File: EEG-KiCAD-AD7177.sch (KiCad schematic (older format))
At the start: 52 parts, among them J1 Conn_01x06, J2 Conn_01x02, J3 Conn_01x02, U1 AD7177-2, U2 OPAMP, U3 NRF528XX-QFAA, U4 RP511Z331_3.3V, U5 XCL101A501-5V, X1 Crystal_GND24, X2 32.768 kHz

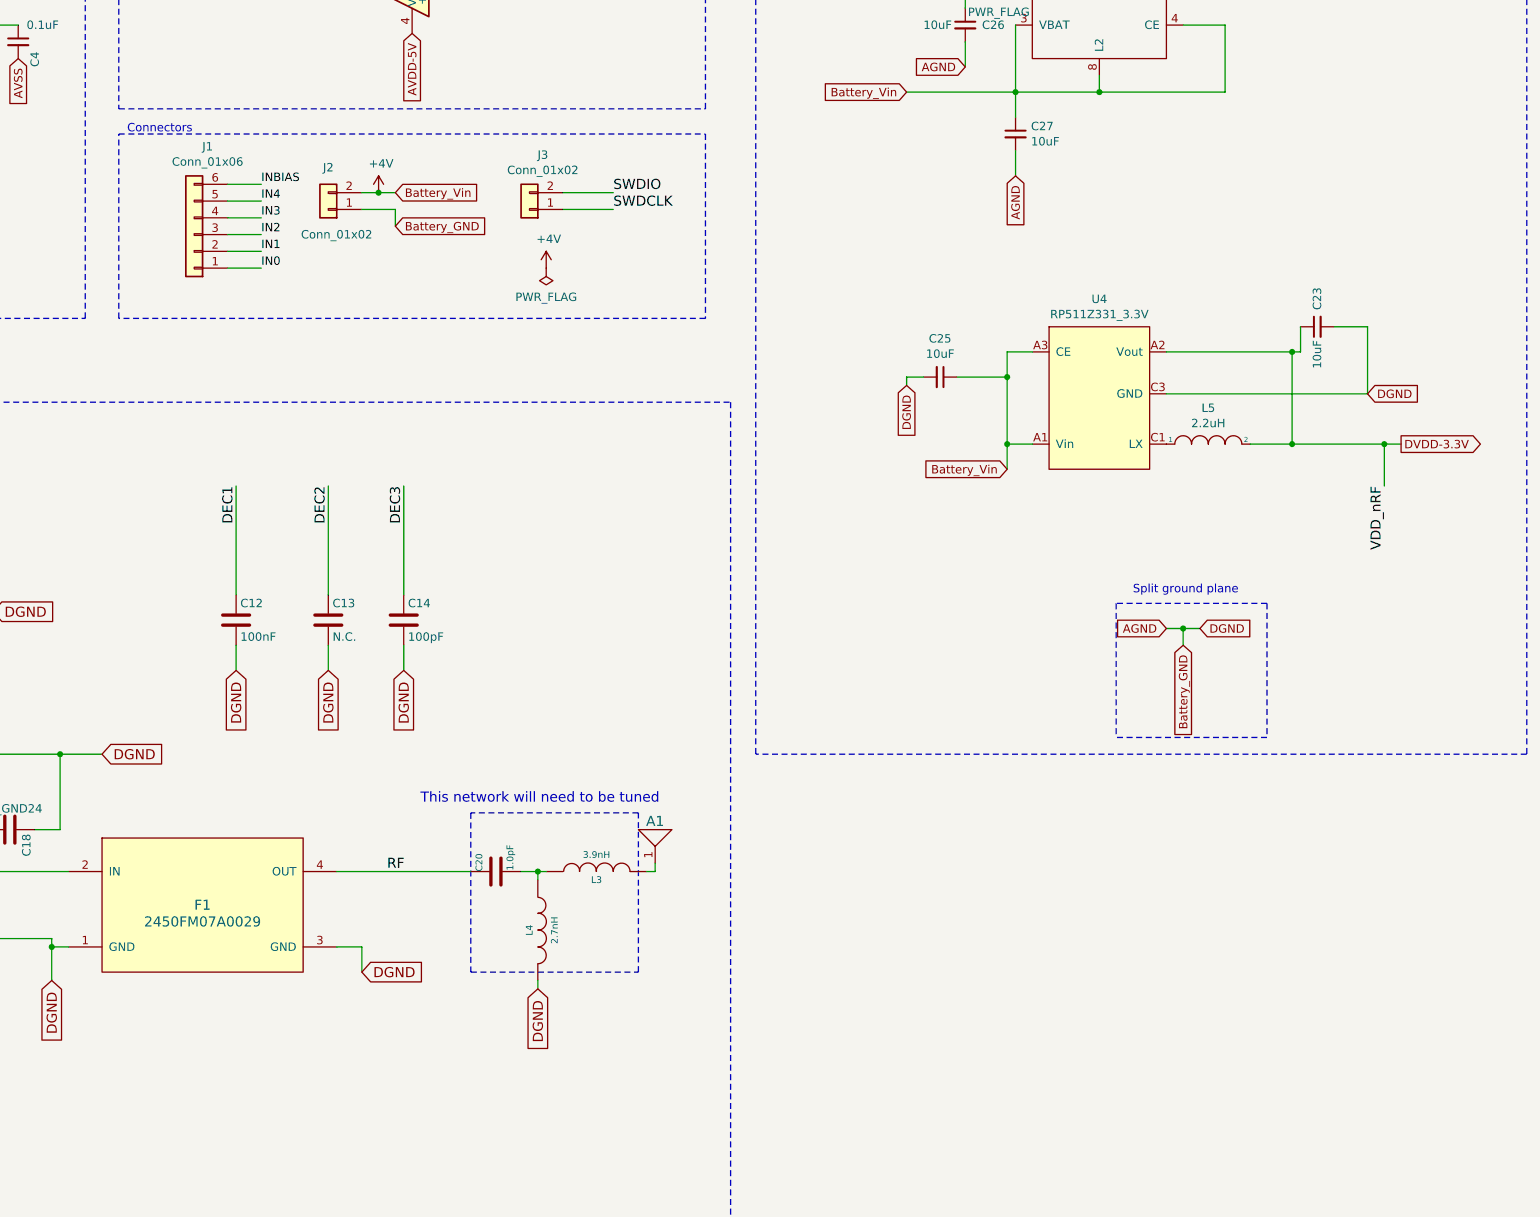
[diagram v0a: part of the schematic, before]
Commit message: Changed with added voltage source
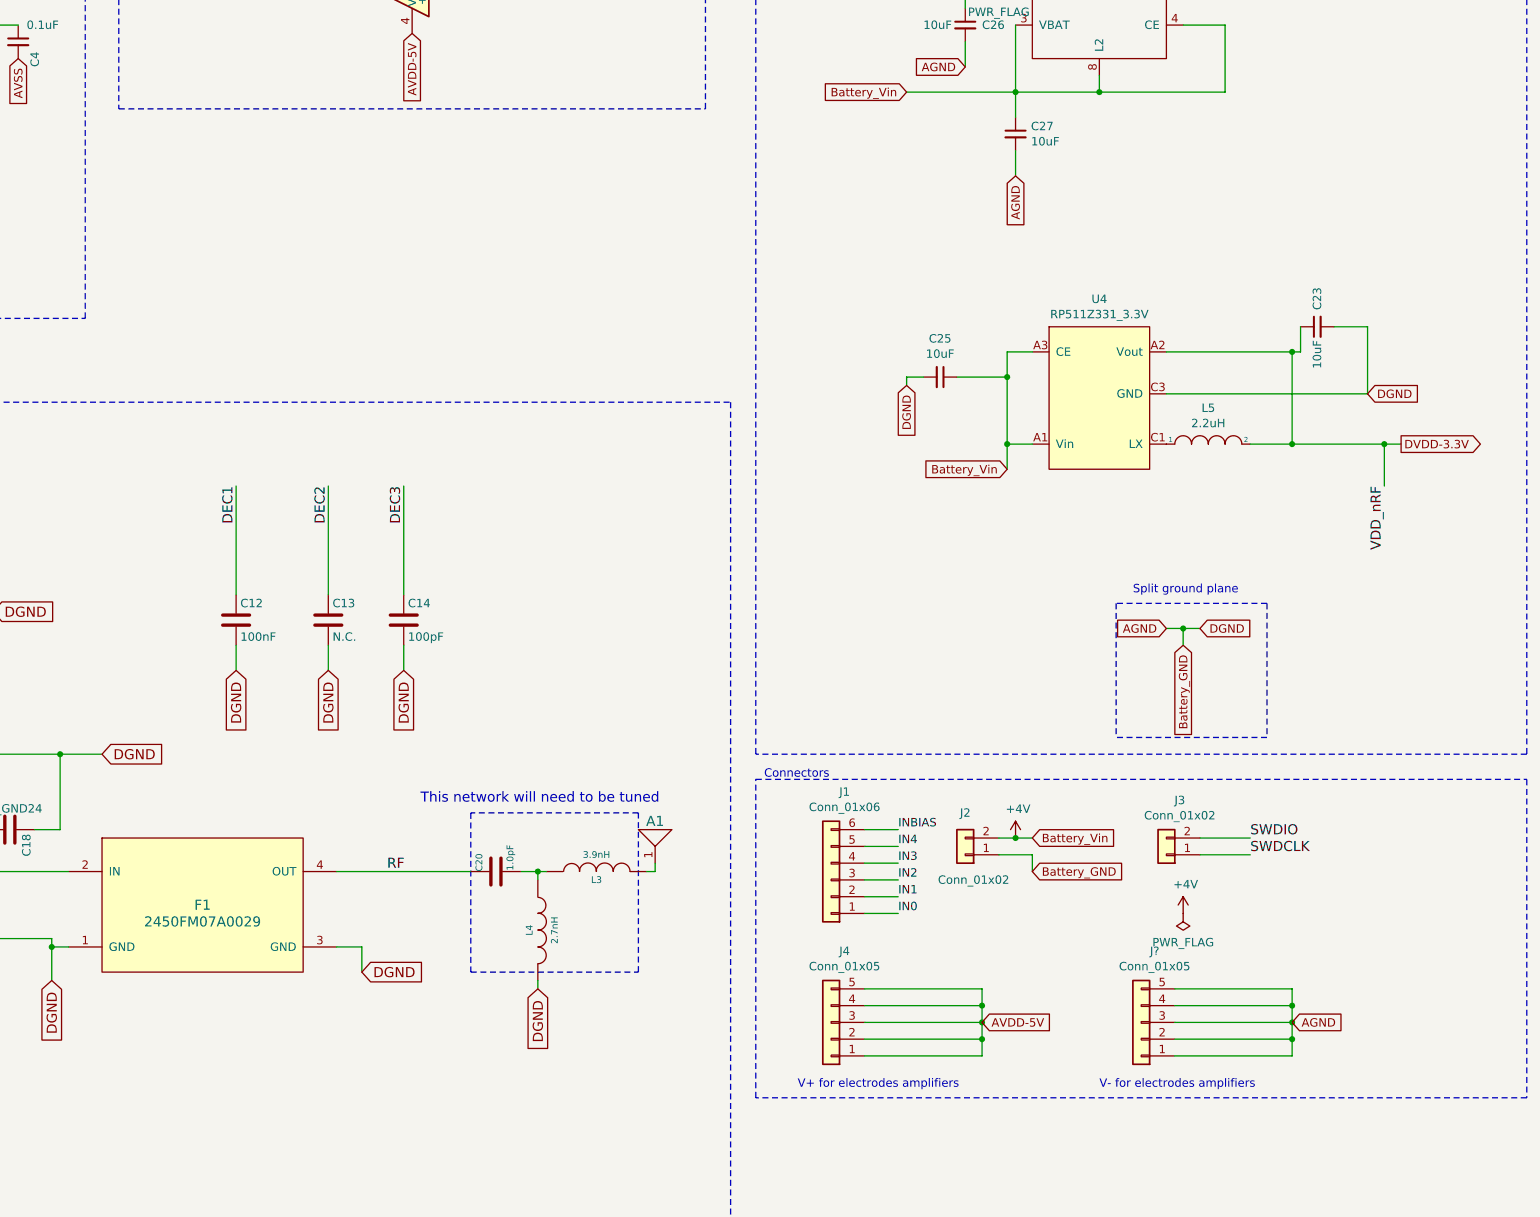
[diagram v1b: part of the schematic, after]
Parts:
- added J4, J?: Conn_01x05, symbol Connector_Generic:Conn_01x05
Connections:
- net AGND: now also J?.1 (Pin_1), J?.2 (Pin_2), J?.3 (Pin_3), J?.4 (Pin_4), J?.5 (Pin_5)
- net AVDD-5V: now also J4.1 (Pin_1), J4.2 (Pin_2), J4.3 (Pin_3), J4.4 (Pin_4), J4.5 (Pin_5)
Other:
- note added: "V+ for electrodes amplifiers\n"
- note added: "V- for electrodes amplifiers\n"
- moved on the sheet: J1, J2, J3
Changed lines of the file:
@@
 L Connector_Generic:Conn_01x06 J1
 U 1 1 5D1C0B90
-P 7650 3750
-F 0 "J1" H 7570 3225 50  0000 C CNN
-F 1 "Conn_01x06" H 7570 3316 50  0000 C CNN
-F 2 "" H 7650 3750 50  0001 C CNN
-F 3 "~" H 7650 3750 50  0001 C CNN
-	1    7650 3750
-	-1   0    0    1
-$EndComp
-Wire Wire Line
-	7850 3450 8050 3450
-Wire Wire Line
-	7850 3550 8050 3550
-Wire Wire Line
-	7850 3650 8050 3650
-Wire Wire Line
-	7850 3750 8050 3750
-Wire Wire Line
-	7850 3850 8050 3850
-Wire Wire Line
-	7850 3950 8050 3950
-Text Label 8050 3550 0    50   ~ 0
+P 11450 7600
+F 0 "J1" H 11370 7075 50  0000 C CNN
+F 1 "Conn_01x06" H 11370 7166 50  0000 C CNN
+F 2 "" H 11450 7600 50  0001 C CNN
+F 3 "~" H 11450 7600 50  0001 C CNN
+	1    11450 7600
+	-1   0    0    1
+$EndComp
+Wire Wire Line
+	11650 7300 11850 7300
+Wire Wire Line
+	11650 7400 11850 7400
+Wire Wire Line
+	11650 7500 11850 7500
+Wire Wire Line
+	11650 7600 11850 7600
+Wire Wire Line
+	11650 7700 11850 7700
+Wire Wire Line
+	11650 7800 11850 7800
+Text Label 11850 7400 0    50   ~ 0
 IN4
-Text Label 8050 3650 0    50   ~ 0
+Text Label 11850 7500 0    50   ~ 0
 IN3
-Text Label 8050 3750 0    50   ~ 0
+Text Label 11850 7600 0    50   ~ 0
 IN2
-Text Label 8050 3850 0    50   ~ 0
+Text Label 11850 7700 0    50   ~ 0
 IN1
-Text Label 8050 3950 0    50   ~ 0
+Text Label 11850 7800 0    50   ~ 0
 IN0
-Text Label 8050 3450 0    50   ~ 0
+Text Label 11850 7300 0    50   ~ 0
 INBIAS
 $Comp
 L Connector_Generic:Conn_01x02 J2
 U 1 1 5D23118E
-P 8450 3600
-F 0 "J2" H 8450 3350 50  0000 C CNN
-F 1 "Conn_01x02" H 8400 3750 50  0000 C CNN
-F 2 "" H 8450 3600 50  0001 C CNN
-F 3 "~" H 8450 3600 50  0001 C CNN
-	1    8450 3600
-	-1   0    0    1
-$EndComp
-Text GLabel 8850 3500 2    50   Input ~ 0
+P 12250 7450
+F 0 "J2" H 12250 7200 50  0000 C CNN
+F 1 "Conn_01x02" H 12200 7600 50  0000 C CNN
+F 2 "" H 12250 7450 50  0001 C CNN
+F 3 "~" H 12250 7450 50  0001 C CNN
+	1    12250 7450
+	-1   0    0    1
+$EndComp
+Text GLabel 12650 7350 2    50   Input ~ 0
 Battery_Vin
 Wire Wire Line
-	8650 3600 8850 3600
-Wire Wire Line
-	8850 3600 8850 3700
-Text GLabel 8850 3700 2    50   Input ~ 0
+	12450 7450 12650 7450
+Wire Wire Line
+	12650 7450 12650 7550
+Text GLabel 12650 7550 2    50   Input ~ 0
 Battery_GND
 $Comp
 L Connector_Generic:Conn_01x02 J3
 U 1 1 5D24B5D1
-P 9650 3600
-F 0 "J3" H 9570 3275 50  0000 C CNN
-F 1 "Conn_01x02" H 9570 3366 50  0000 C CNN
-F 2 "" H 9650 3600 50  0001 C CNN
-F 3 "~" H 9650 3600 50  0001 C CNN
-	1    9650 3600
-	-1   0    0    1
-$EndComp
-Wire Wire Line
-	9850 3500 10150 3500
-Text Label 10150 3500 0    60   ~ 0
+P 13450 7450
+F 0 "J3" H 13370 7125 50  0000 C CNN
+F 1 "Conn_01x02" H 13370 7216 50  0000 C CNN
+F 2 "" H 13450 7450 50  0001 C CNN
+F 3 "~" H 13450 7450 50  0001 C CNN
+	1    13450 7450
+	-1   0    0    1
+$EndComp
+Wire Wire Line
+	13650 7350 13950 7350
+Text Label 13950 7350 0    60   ~ 0
 SWDIO
-Text Label 10150 3600 0    60   ~ 0
+Text Label 13950 7450 0    60   ~ 0
 SWDCLK
 Wire Wire Line
-	9850 3600 10150 3600
-Wire Notes Line
-	7200 3150 10700 3150
-Wire Notes Line
-	10700 3150 10700 4250
-Wire Notes Line
-	10700 4250 7200 4250
-Wire Notes Line
-	7200 4250 7200 3150
-Text Notes 7250 3150 0    50   ~ 0
+	13650 7450 13950 7450
+Wire Notes Line
+	11000 7000 15600 7000
+Wire Notes Line
+	15600 7000 15600 8900
+Wire Notes Line
+	15600 8900 11000 8900
+Wire Notes Line
+	11000 8900 11000 7000
+Text Notes 11050 7000 0    50   ~ 0
 Connectors\n
 NoConn ~ 5650 8150
@@
 	10250 2150 10250 1800
 Wire Wire Line
-	8650 3500 8750 3500
+	12450 7350 12550 7350
 $Comp
 L power:+4V #PWR0101
 U 1 1 5D519D32
-P 8750 3500
-F 0 "#PWR0101" H 8750 3350 50  0001 C CNN
-F 1 "+4V" H 8765 3673 50  0000 C CNN
-F 2 "" H 8750 3500 50  0001 C CNN
-F 3 "" H 8750 3500 50  0001 C CNN
-	1    8750 3500
+P 12550 7350
+F 0 "#PWR0101" H 12550 7200 50  0001 C CNN
+F 1 "+4V" H 12565 7523 50  0000 C CNN
+F 2 "" H 12550 7350 50  0001 C CNN
+F 3 "" H 12550 7350 50  0001 C CNN
+	1    12550 7350
 	1    0    0    -1
 $EndComp
-Connection ~ 8750 3500
-Wire Wire Line
-	8750 3500 8850 3500
+Connection ~ 12550 7350
+Wire Wire Line
+	12550 7350 12650 7350
 $Comp
 L power:+4V #PWR0102
 U 1 1 5D527820
-P 9750 3950
-F 0 "#PWR0102" H 9750 3800 50  0001 C CNN
-F 1 "+4V" H 9765 4123 50  0000 C CNN
-F 2 "" H 9750 3950 50  0001 C CNN
-F 3 "" H 9750 3950 50  0001 C CNN
-	1    9750 3950
+P 13550 7800
+F 0 "#PWR0102" H 13550 7650 50  0001 C CNN
+F 1 "+4V" H 13565 7973 50  0000 C CNN
+F 2 "" H 13550 7800 50  0001 C CNN
+F 3 "" H 13550 7800 50  0001 C CNN
+	1    13550 7800
 	1    0    0    -1
 $EndComp
@@
 L power:PWR_FLAG #FLG0101
 U 1 1 5D52792B
-P 9750 3950
-F 0 "#FLG0101" H 9750 4025 50  0001 C CNN
-F 1 "PWR_FLAG" H 9750 4123 50  0000 C CNN
-F 2 "" H 9750 3950 50  0001 C CNN
-F 3 "~" H 9750 3950 50  0001 C CNN
-	1    9750 3950
+P 13550 7800
+F 0 "#FLG0101" H 13550 7875 50  0001 C CNN
+F 1 "PWR_FLAG" H 13550 7973 50  0000 C CNN
+F 2 "" H 13550 7800 50  0001 C CNN
+F 3 "~" H 13550 7800 50  0001 C CNN
+	1    13550 7800
 	-1   0    0    1
 $EndComp
@@
 Wire Wire Line
 	14200 5000 14750 5000
+$Comp
+L Connector_Generic:Conn_01x05 J4
+U 1 1 5CBA8A87
+P 11450 8450
+F 0 "J4" H 11370 8025 50  0000 C CNN
+F 1 "Conn_01x05" H 11370 8116 50  0000 C CNN
+F 2 "" H 11450 8450 50  0001 C CNN
+F 3 "~" H 11450 8450 50  0001 C CNN
+	1    11450 8450
+	-1   0    0    1
+$EndComp
+Text GLabel 12350 8450 2    50   Input ~ 0
+AVDD-5V
+Wire Wire Line
+	11650 8250 12350 8250
+Wire Wire Line
+	11650 8350 12350 8350
+Wire Wire Line
+	12350 8250 12350 8350
+Connection ~ 12350 8350
+Wire Wire Line
+	11650 8450 12350 8450
+Wire Wire Line
+	12350 8350 12350 8450
+Wire Wire Line
+	11650 8550 12350 8550
+Wire Wire Line
+	12350 8550 12350 8450
+Connection ~ 12350 8450
+Wire Wire Line
+	11650 8650 12350 8650
+Wire Wire Line
+	12350 8650 12350 8550
+Connection ~ 12350 8550
+Text Notes 11250 8850 0    50   ~ 0
+V+ for electrodes amplifiers\n
+$Comp
+L Connector_Generic:Conn_01x05 J?
+U 1 1 5CBF02C9
+P 13300 8450
+F 0 "J?" H 13220 8025 50  0000 C CNN
+F 1 "Conn_01x05" H 13220 8116 50  0000 C CNN
+F 2 "" H 13300 8450 50  0001 C CNN
+F 3 "~" H 13300 8450 50  0001 C CNN
+	1    13300 8450
+	-1   0    0    1
+$EndComp
+Wire Wire Line
+	13500 8250 14200 8250
+Wire Wire Line
+	13500 8350 14200 8350
+Wire Wire Line
+	14200 8250 14200 8350
+Connection ~ 14200 8350
+Wire Wire Line
+	13500 8450 14200 8450
+Wire Wire Line
+	14200 8350 14200 8450
+Wire Wire Line
+	13500 8550 14200 8550
+Wire Wire Line
+	14200 8550 14200 8450
+Connection ~ 14200 8450
+Wire Wire Line
+	13500 8650 14200 8650
+Wire Wire Line
+	14200 8650 14200 8550
+Connection ~ 14200 8550
+Text GLabel 14200 8450 2    50   Input ~ 0
+AGND
+Text Notes 13050 8850 0    50   ~ 0
+V- for electrodes amplifiers\n
 $EndSCHEMATC
